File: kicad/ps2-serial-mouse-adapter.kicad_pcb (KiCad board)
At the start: 2 copper layers, 60.3 x 31.1 mm, 11 parts, among them U1 Arduino_Mini, U2 MAX232

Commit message: Replace DB9 by DB9_mounting_holes
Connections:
- RS232 pad 0: (no net) -> GND

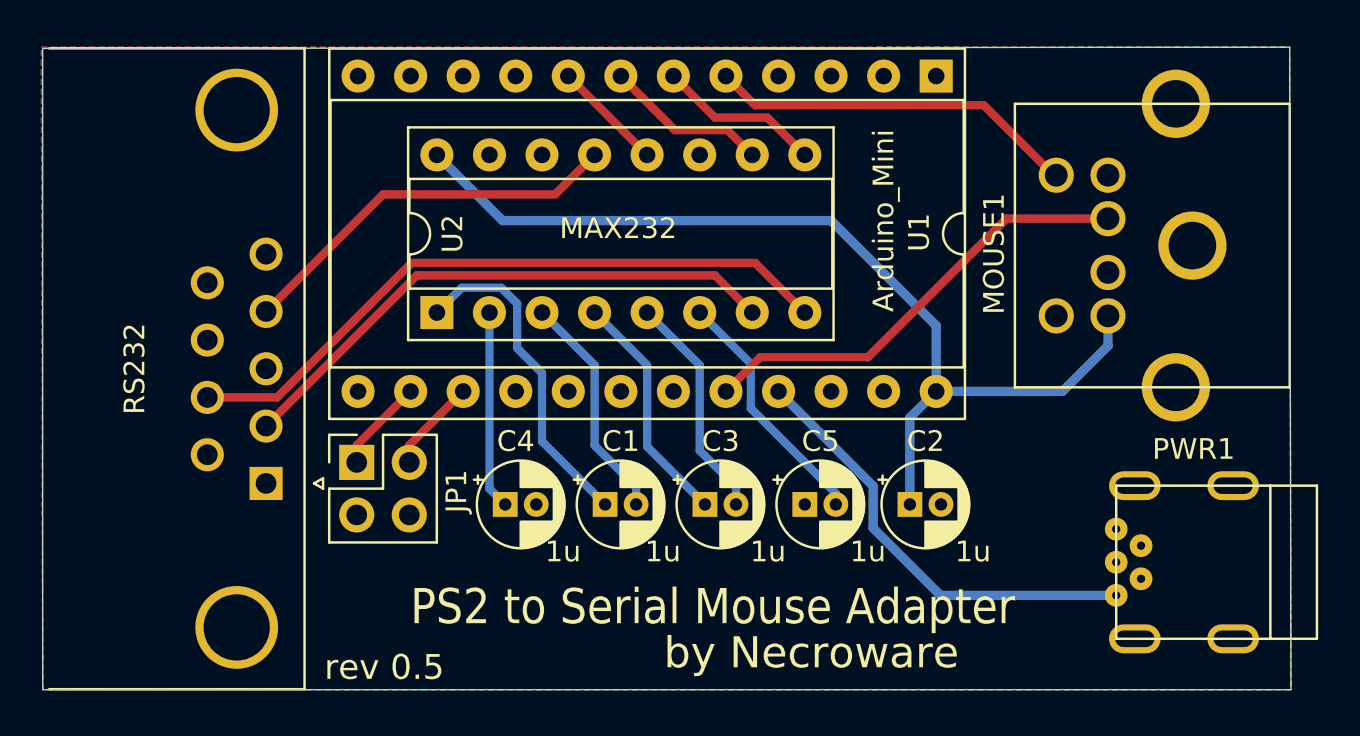
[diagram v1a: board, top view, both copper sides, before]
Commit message: Fix wrong VCC network
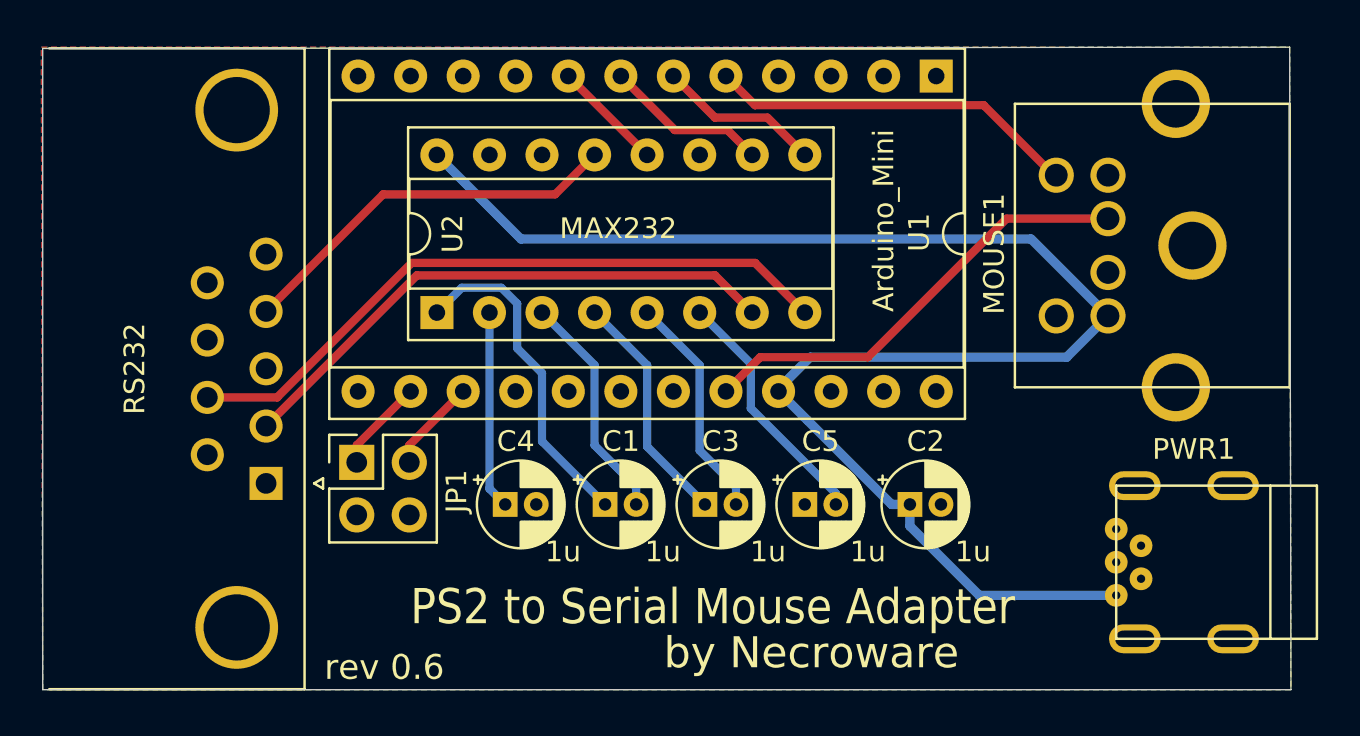
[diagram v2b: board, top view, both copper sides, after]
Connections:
- PWR1 pad 1: VCC -> Net-(C2-Pad1)
- U1 pad 21: VCC -> Net-(C2-Pad1)
- U1 pad 24: Net-(C2-Pad1) -> (no net)
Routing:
- net Net-(C2-Pad1): track 47.4 -> 74.2 mm
- net VCC: track 21.6 -> 0.00 mm
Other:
- board text added: "rev 0.6"
- board text removed: "rev 0.5"

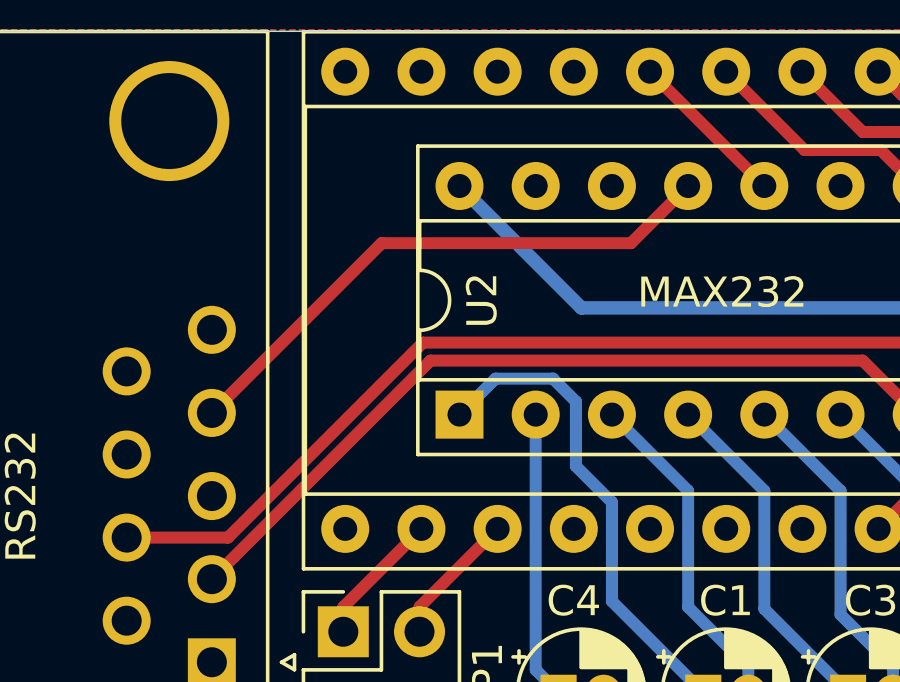
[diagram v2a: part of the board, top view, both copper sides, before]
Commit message: Replace serial DTR through TX.
DTR was not used anyway and TX can be used in the future for
communication with the adapter through serial port
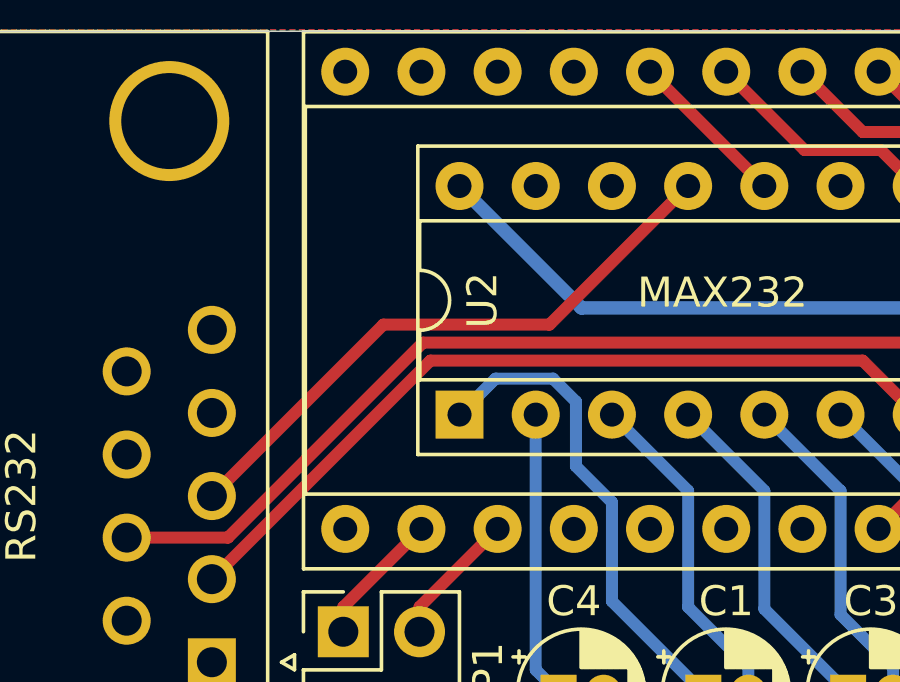
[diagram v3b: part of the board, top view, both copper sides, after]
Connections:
- net DTS renamed RX
- RS232 pad 3: (no net) -> Net-(RS232-Pad3)
- RS232 pad 4: Net-(RS232-Pad4) -> (no net)
- U2 pad 13: Net-(RS232-Pad4) -> Net-(RS232-Pad3)
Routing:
- net Net-(RS232-Pad3): track 0.00 -> 20.2 mm
- net Net-(RS232-Pad4): track 19.0 -> 0.00 mm

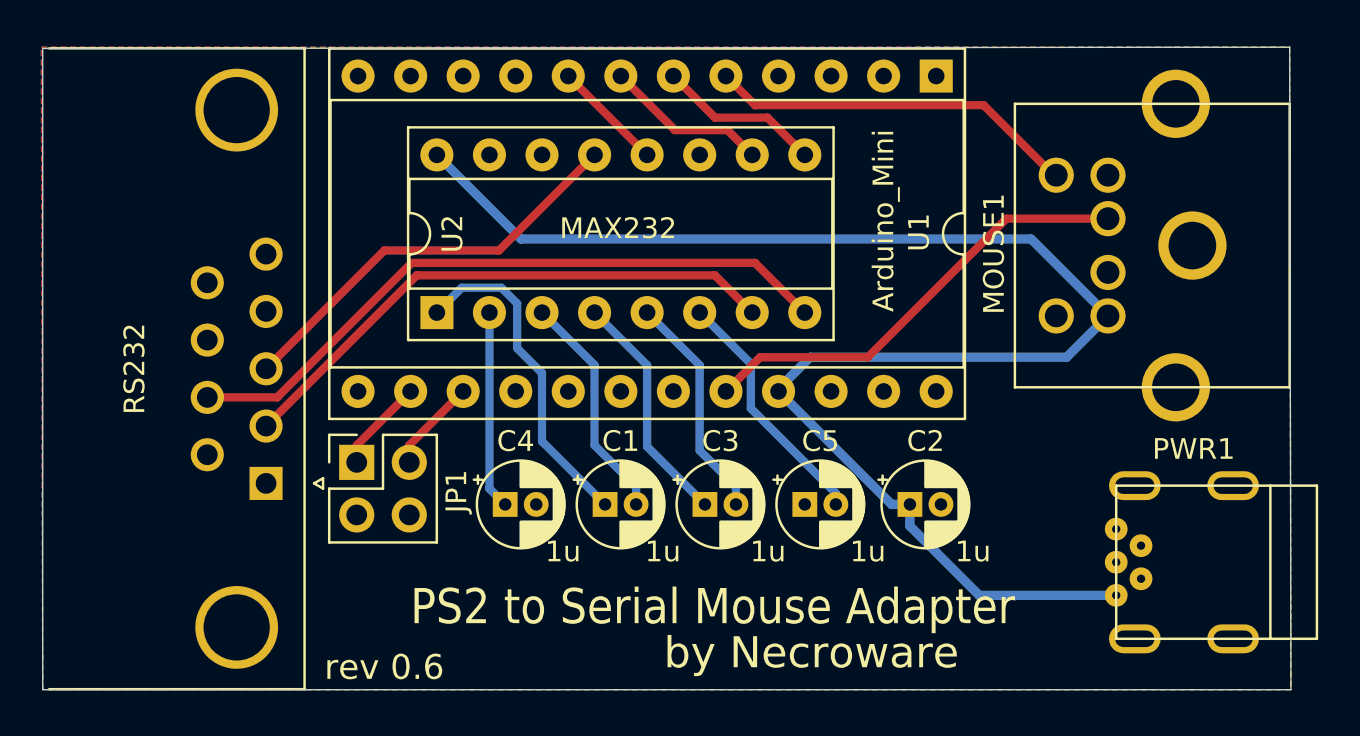
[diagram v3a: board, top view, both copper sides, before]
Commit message: Add a pull-up resistor to the ps/2 clock
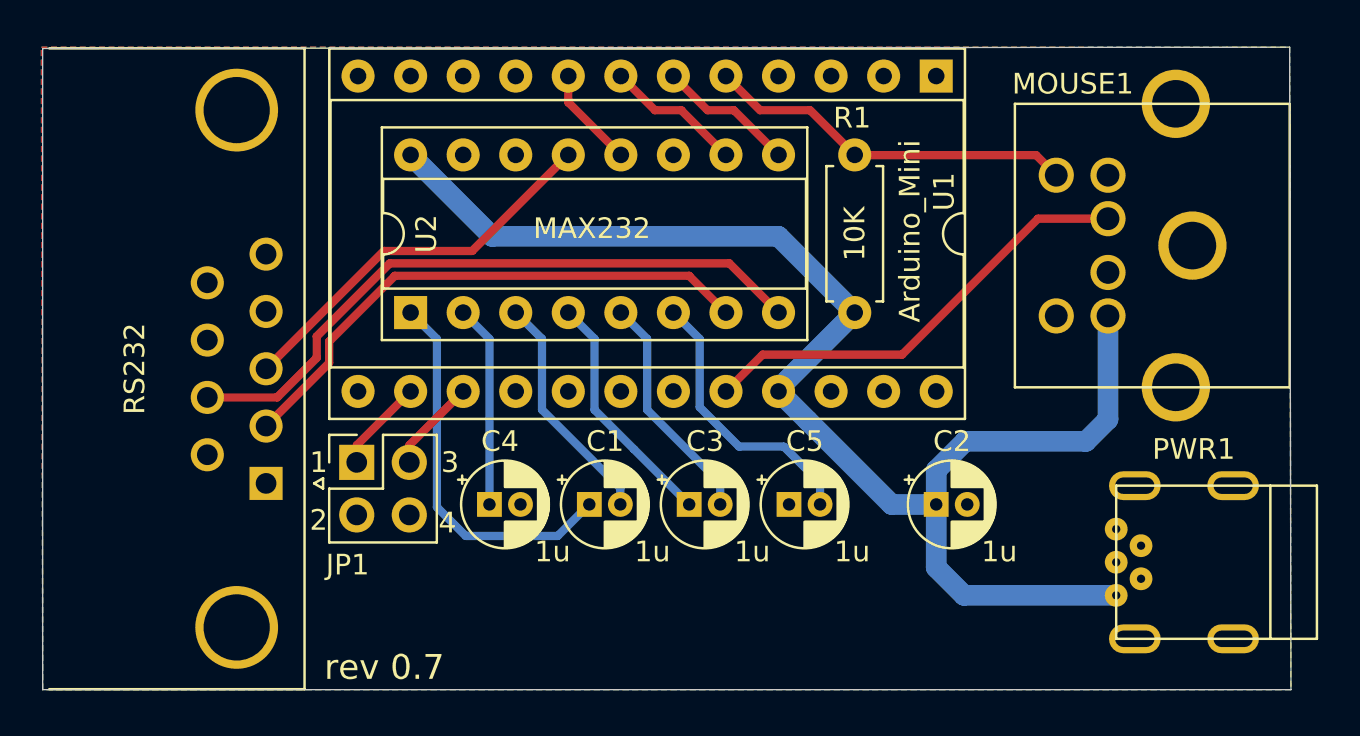
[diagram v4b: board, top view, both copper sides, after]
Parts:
- added R1: 10K, Resistor_THT:R_Axial_DIN0207_L6.3mm_D2.5mm_P7.62mm_Horizontal, F.Cu at (120.5, 67.9)
- moved C2 1.27 mm to (124.5, 77.2)
- moved U2 1.27 mm to (99.1, 67.9)
- moved C1 0.76 mm to (107.7, 77.2)
- moved C3 0.76 mm to (112.5, 77.2)
- moved C4 0.76 mm to (102.9, 77.2)
- moved C5 0.76 mm to (117.3, 77.2)
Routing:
- net Net-(C2-Pad1): track 74.2 -> 68.1 mm
- net Net-(C1-Pad1): track 16.3 -> 18.5 mm
- net Net-(C5-Pad2): track 12.0 -> 13.5 mm
- net RTS: track 7.93 -> 6.66 mm
- net Net-(RS232-Pad3): track 20.2 -> 18.9 mm
- net TX: track 7.93 -> 6.66 mm
- net Net-(RS232-Pad2): track 27.3 -> 26.6 mm
- net Net-(RS232-Pad7): track 32.6 -> 31.9 mm
- net RX: track 5.39 -> 4.86 mm
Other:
- net class Power: trace_width 0.45 -> 1
- board text added: "rev 0.7"
- board text removed: "rev 0.6"

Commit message: Updated project to KiCad 6.0.x
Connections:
- MOUSE1 pad 2: (no net) -> unconnected-(MOUSE1-Pad2)
- MOUSE1 pad 6: (no net) -> unconnected-(MOUSE1-Pad6)
- PWR1 pad 2: (no net) -> unconnected-(PWR1-Pad2)
- PWR1 pad 3: (no net) -> unconnected-(PWR1-Pad3)
- PWR1 pad 4: (no net) -> unconnected-(PWR1-Pad4)
- RS232 pad 1: (no net) -> unconnected-(RS232-Pad1)
- RS232 pad 4: (no net) -> unconnected-(RS232-Pad4)
- RS232 pad 6: (no net) -> unconnected-(RS232-Pad6)
- RS232 pad 8: (no net) -> unconnected-(RS232-Pad8)
- RS232 pad 9: (no net) -> unconnected-(RS232-Pad9)
- U1 pad 1: (no net) -> unconnected-(U1-Pad1)
- U1 pad 10: (no net) -> unconnected-(U1-Pad10)
- U1 pad 11: (no net) -> unconnected-(U1-Pad11)
- U1 pad 12: (no net) -> unconnected-(U1-Pad12)
- U1 pad 13: (no net) -> unconnected-(U1-Pad13)
- U1 pad 16: (no net) -> unconnected-(U1-Pad16)
- U1 pad 17: (no net) -> unconnected-(U1-Pad17)
- U1 pad 18: (no net) -> unconnected-(U1-Pad18)
- U1 pad 19: (no net) -> unconnected-(U1-Pad19)
- U1 pad 2: (no net) -> unconnected-(U1-Pad2)
- U1 pad 22: (no net) -> unconnected-(U1-Pad22)
- U1 pad 24: (no net) -> unconnected-(U1-Pad24)
- U1 pad 3: (no net) -> unconnected-(U1-Pad3)
- U1 pad 9: (no net) -> unconnected-(U1-Pad9)
- U2 pad 11: (no net) -> unconnected-(U2-Pad11)
- U2 pad 14: (no net) -> unconnected-(U2-Pad14)
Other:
- net class Default removed
- net class Power removed

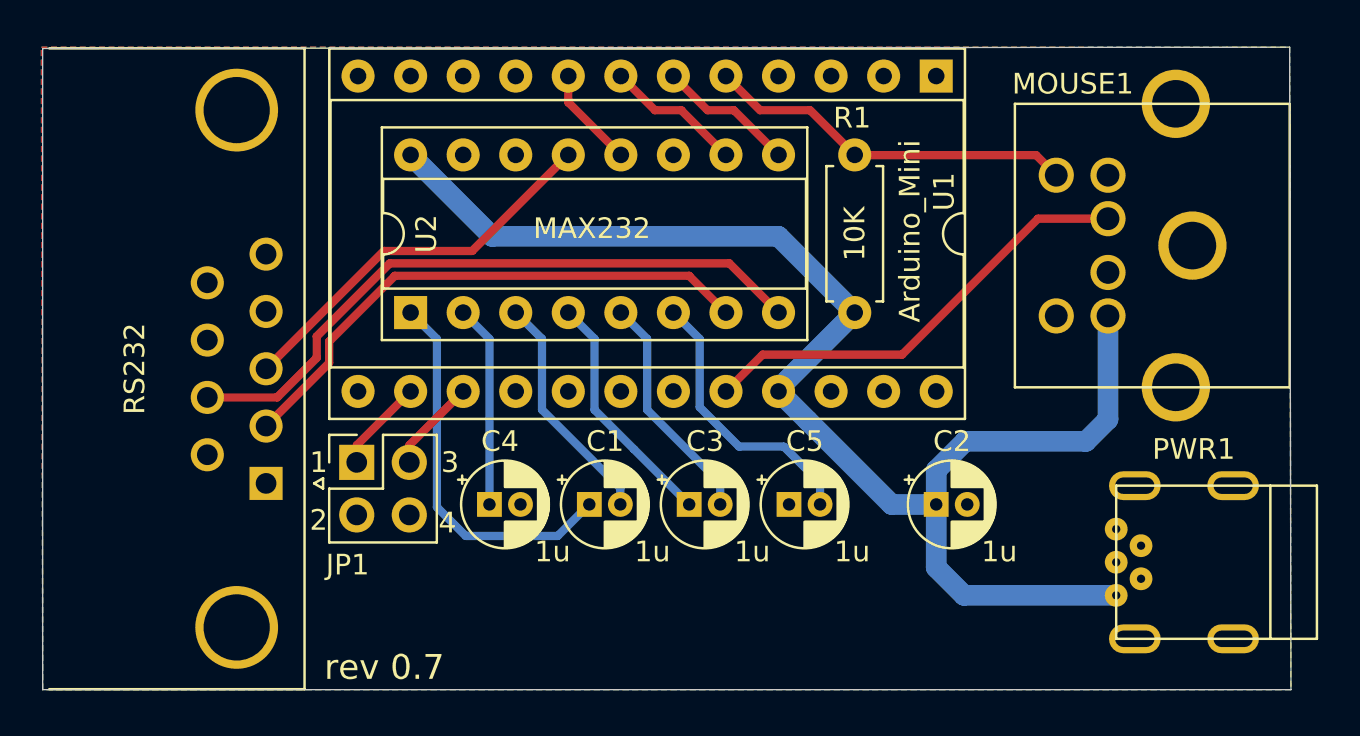
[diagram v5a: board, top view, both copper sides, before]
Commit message: Switched charge pump from GND to VCC
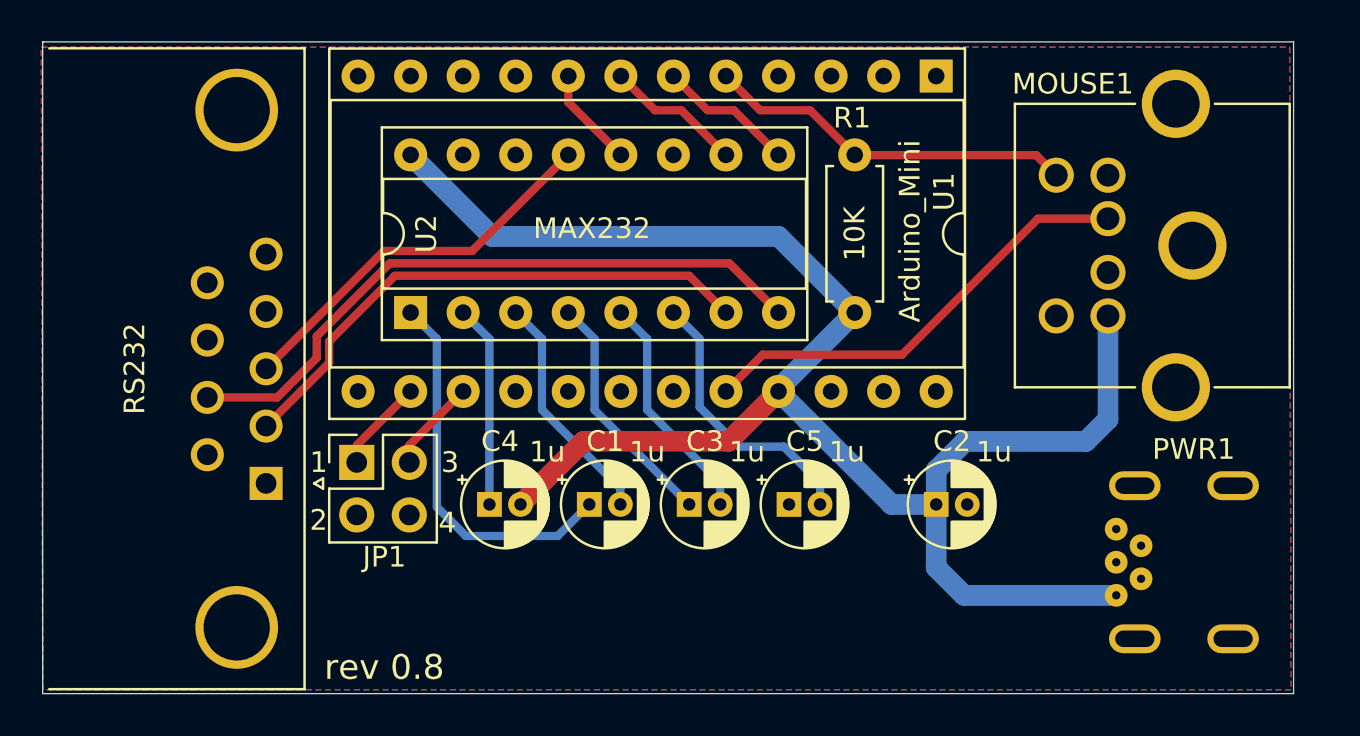
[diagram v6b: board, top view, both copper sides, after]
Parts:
- added REF**: OSHW-Symbol_6.7x6mm_SilkScreen, Symbol:OSHW-Symbol_6.7x6mm_SilkScreen, F.Cu at (128.0, 82.5)
- MOUSE1: footprint Necroware:Mini_DIN_6_LCSC_C77848 -> ps2-serial-mouse-adapter:Mini_DIN_6_LCSC_C77848
- PWR1: footprint MyLibrary:USB_Mini-B-Jing_Extension_LSCS_C46398 -> ps2-serial-mouse-adapter:USB_Mini-B-Jing_Extension_LSCS_C46398
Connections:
- C4 pad 2: GND -> Net-(C2-Pad1)
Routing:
- net Net-(C2-Pad1): track 68.1 -> 82.8 mm
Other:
- board size 60.3 x 31.1 mm -> 60.5 x 31.5 mm
- board text added: "rev 0.8"
- board text removed: "rev 0.7"

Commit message: Warnings fixed
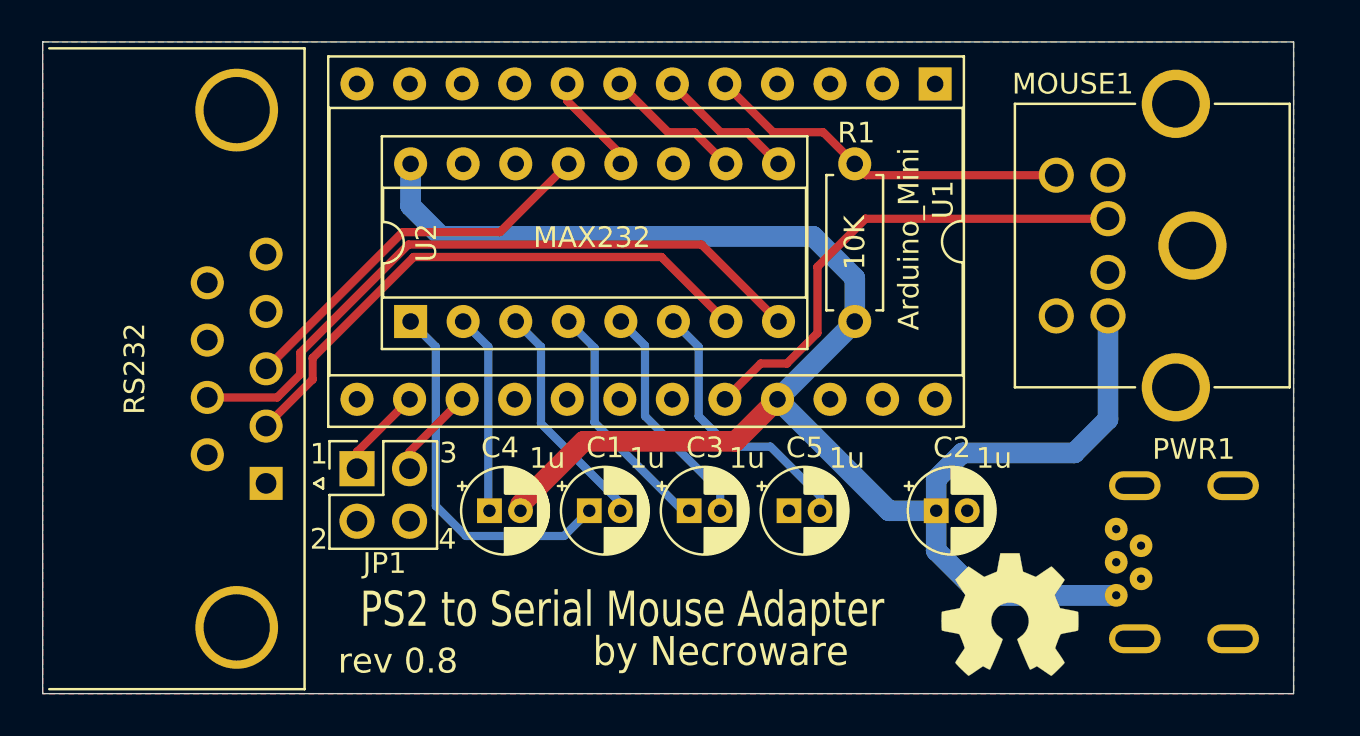
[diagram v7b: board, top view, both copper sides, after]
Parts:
- moved R1 0.43 mm to (120.5, 68.4)
- moved U2 0.43 mm to (99.1, 68.4)
- moved U1 0.38 mm to (124.4, 56.9)
- moved JP1 0.31 mm to (96.5, 75.5)
- moved C1 0.30 mm to (107.7, 77.5)
- moved C2 0.30 mm to (124.5, 77.5)
- moved C3 0.30 mm to (112.5, 77.5)
- moved C4 0.30 mm to (102.9, 77.5)
- moved C5 0.30 mm to (117.3, 77.5)
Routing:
- net DATA: track 21.9 -> 24.0 mm
- net Net-(PWR1-VBUS): track 82.8 -> 84.3 mm
- net Net-(U2-T2OUT): track 26.6 -> 27.5 mm
- net Net-(U2-R2IN): track 31.9 -> 32.8 mm
- net Net-(U2-C1+): track 18.5 -> 17.9 mm
